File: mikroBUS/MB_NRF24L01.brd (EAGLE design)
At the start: 49.2 x 27.9 mm, 2 parts

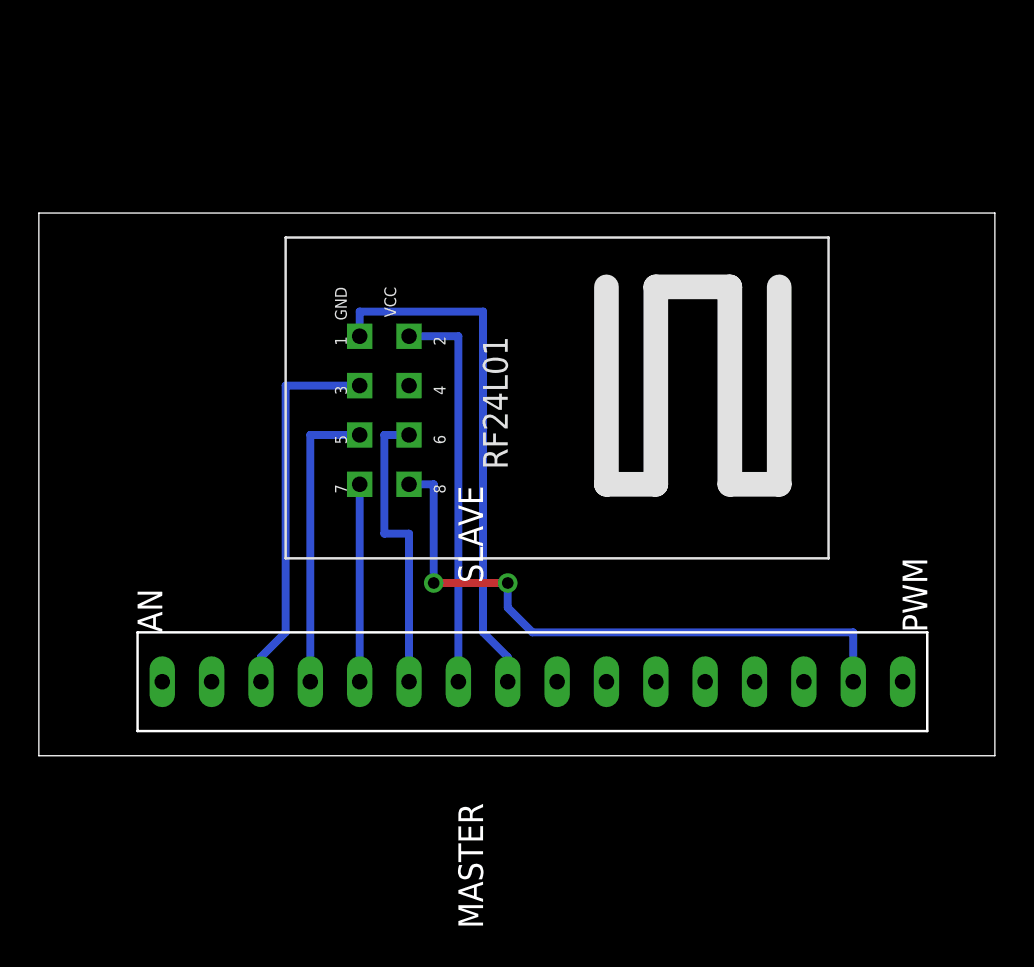
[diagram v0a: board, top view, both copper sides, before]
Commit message: 
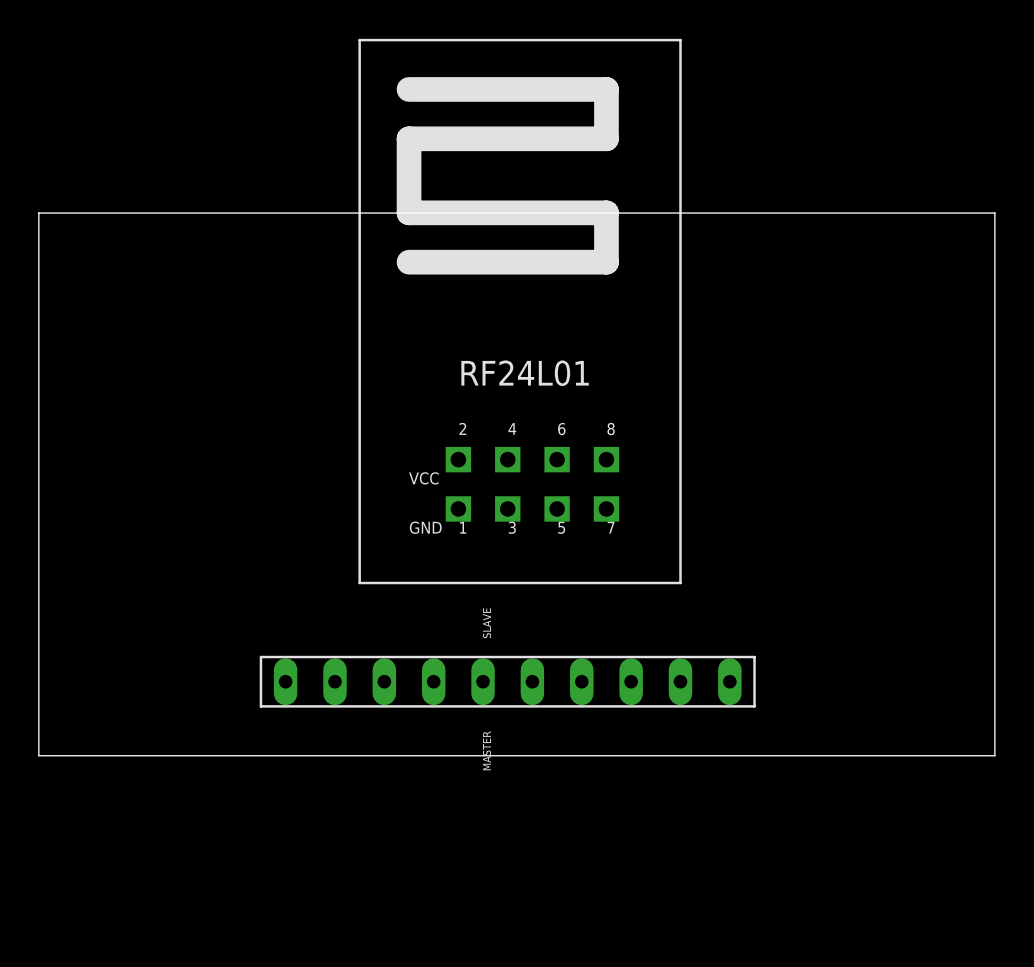
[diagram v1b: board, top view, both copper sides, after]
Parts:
- U$1: value (none) -> SPI_BUS; device lieven:MIKROBUS_SIL -> lieven:SPI_BUS
- moved U$1 11.4 mm to (35.6, 3.81), turned to 270 degrees
- moved U$2 10.2 mm to (44.5, 12.7), turned to 0 degrees
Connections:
- removed net N$3 (its old number): U$1.CS, U$2.P$3
- new net N$6: U$1.CS, U$2.P$4
- new net N$8: U$1.GPIO, U$2.P$3
- net N$2: now also U$1.+3V3; no longer U$1.+3.3V
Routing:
- net N$7: track 32.3 -> 0.00 mm, vias 2 -> 0
- net N$1: track 27.2 -> 0.00 mm
- net N$2: track 20.3 -> 0.00 mm
- net N$3 (its old number): track 19.6 -> 0.00 mm
- net N$5: track 15.2 -> 0.00 mm
- net N$3: track 15.2 -> 0.00 mm
- net N$4: track 10.2 -> 0.00 mm
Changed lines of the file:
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@@
 </autorouter>
 <elements>
-<element name="U$1" library="lieven" package="MIKROBUS_SIL" value="" x="46.99" y="3.81" rot="R90"/>
-<element name="U$2" library="lieven" package="ML8" value="RF24L01MODULE" x="39.37" y="21.59" rot="R270"/>
+<element name="U$2" library="lieven" package="ML8" value="RF24L01MODULE" x="44.45" y="12.7"/>
+<element name="U$1" library="lieven" package="SPI_BUS" value="SPI_BUS" x="35.56" y="3.81" rot="R270"/>
 </elements>
 <signals>
@@
 <contactref element="U$2" pad="P$1"/>
 <contactref element="U$1" pad="GND"/>
-<wire x1="39.37" y1="21.59" x2="39.37" y2="22.86" width="0.4064" layer="16"/>
-<wire x1="39.37" y1="22.86" x2="45.72" y2="22.86" width="0.4064" layer="16"/>
-<wire x1="45.72" y1="22.86" x2="45.72" y2="6.35" width="0.4064" layer="16"/>
-<wire x1="45.72" y1="6.35" x2="46.99" y2="5.08" width="0.4064" layer="16"/>
-<wire x1="46.99" y1="5.08" x2="46.99" y2="3.81" width="0.4064" layer="16"/>
+<wire x1="35.56" y1="3.81" x2="44.45" y2="12.7" width="0" layer="19" extent="1-1"/>
 </signal>
 <signal name="N$2">
 <contactref element="U$2" pad="P$2"/>
-<contactref element="U$1" pad="+3.3V"/>
-<wire x1="44.45" y1="3.81" x2="44.45" y2="21.59" width="0.4064" layer="16"/>
-<wire x1="44.45" y1="21.59" x2="41.91" y2="21.59" width="0.4064" layer="16"/>
+<contactref element="U$1" pad="+3V3"/>
+<wire x1="38.1" y1="3.81" x2="44.45" y2="15.24" width="0" layer="19" extent="1-1"/>
 </signal>
 <signal name="N$3">
-<contactref element="U$2" pad="P$3"/>
-<contactref element="U$1" pad="CS"/>
-<wire x1="34.29" y1="3.81" x2="34.29" y2="5.08" width="0.4064" layer="16"/>
-<wire x1="34.29" y1="5.08" x2="35.56" y2="6.35" width="0.4064" layer="16"/>
-<wire x1="35.56" y1="6.35" x2="35.56" y2="19.05" width="0.4064" layer="16"/>
-<wire x1="35.56" y1="19.05" x2="39.37" y2="19.05" width="0.4064" layer="16"/>
+<contactref element="U$2" pad="P$6"/>
+<contactref element="U$1" pad="MOSI"/>
+<wire x1="43.18" y1="3.81" x2="49.53" y2="15.24" width="0" layer="19" extent="1-1"/>
 </signal>
 <signal name="N$4">
 <contactref element="U$2" pad="P$7"/>
 <contactref element="U$1" pad="MISO"/>
-<wire x1="39.37" y1="3.81" x2="39.37" y2="13.97" width="0.4064" layer="16"/>
+<wire x1="45.72" y1="3.81" x2="52.07" y2="12.7" width="0" layer="19" extent="1-1"/>
 </signal>
 <signal name="N$5">
-<contactref element="U$2" pad="P$6"/>
-<contactref element="U$1" pad="MOSI"/>
-<wire x1="41.91" y1="3.81" x2="41.91" y2="11.43" width="0.4064" layer="16"/>
-<wire x1="41.91" y1="11.43" x2="40.64" y2="11.43" width="0.4064" layer="16"/>
-<wire x1="40.64" y1="11.43" x2="40.64" y2="16.51" width="0.4064" layer="16"/>
-<wire x1="40.64" y1="16.51" x2="41.91" y2="16.51" width="0.4064" layer="16"/>
+<contactref element="U$2" pad="P$5"/>
+<contactref element="U$1" pad="SCK"/>
+<wire x1="48.26" y1="3.81" x2="49.53" y2="12.7" width="0" layer="19" extent="1-1"/>
 </signal>
 <signal name="N$6">
-<contactref element="U$2" pad="P$5"/>
-<contactref element="U$1" pad="SCK"/>
-<wire x1="39.37" y1="16.51" x2="36.83" y2="16.51" width="0.4064" layer="16"/>
-<wire x1="36.83" y1="16.51" x2="36.83" y2="3.81" width="0.4064" layer="16"/>
+<contactref element="U$2" pad="P$4"/>
+<contactref element="U$1" pad="CS"/>
+<wire x1="50.8" y1="3.81" x2="46.99" y2="15.24" width="0" layer="19" extent="1-1"/>
 </signal>
 <signal name="N$7">
 <contactref element="U$2" pad="P$8"/>
 <contactref element="U$1" pad="INT"/>
-<wire x1="41.91" y1="13.97" x2="43.18" y2="13.97" width="0.4064" layer="16"/>
-<wire x1="43.18" y1="13.97" x2="43.18" y2="8.89" width="0.4064" layer="16"/>
-<wire x1="43.18" y1="8.89" x2="46.99" y2="8.89" width="0.4064" layer="1"/>
-<wire x1="46.99" y1="8.89" x2="46.99" y2="7.62" width="0.4064" layer="16"/>
-<wire x1="46.99" y1="7.62" x2="48.26" y2="6.35" width="0.4064" layer="16"/>
-<wire x1="48.26" y1="6.35" x2="64.77" y2="6.35" width="0.4064" layer="16"/>
-<wire x1="64.77" y1="6.35" x2="64.77" y2="3.81" width="0.4064" layer="16"/>
-<via x="43.18" y="8.89" extent="1-16" drill="0.6" shape="square"/>
-<via x="46.99" y="8.89" extent="1-16" drill="0.6" shape="square"/>
+<wire x1="53.34" y1="3.81" x2="52.07" y2="15.24" width="0" layer="19" extent="1-1"/>
+</signal>
+<signal name="N$8">
+<contactref element="U$2" pad="P$3"/>
+<contactref element="U$1" pad="GPIO"/>
+<wire x1="46.99" y1="12.7" x2="58.42" y2="3.81" width="0" layer="19" extent="1-1"/>
 </signal>
 </signals>
